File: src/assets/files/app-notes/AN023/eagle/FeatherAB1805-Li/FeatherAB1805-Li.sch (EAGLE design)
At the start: 11 parts, among them Q1 32.768kHz, Q2 2N7002L, U1 XC6215, U2 AB1805

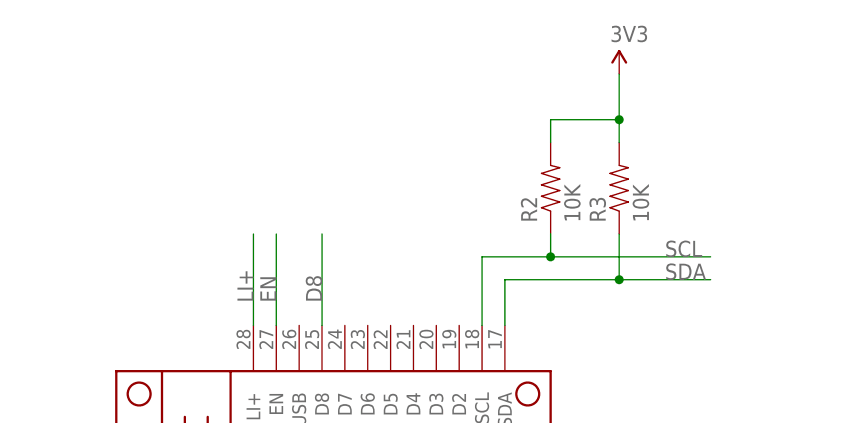
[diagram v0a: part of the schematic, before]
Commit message: Update AB1805-Li design
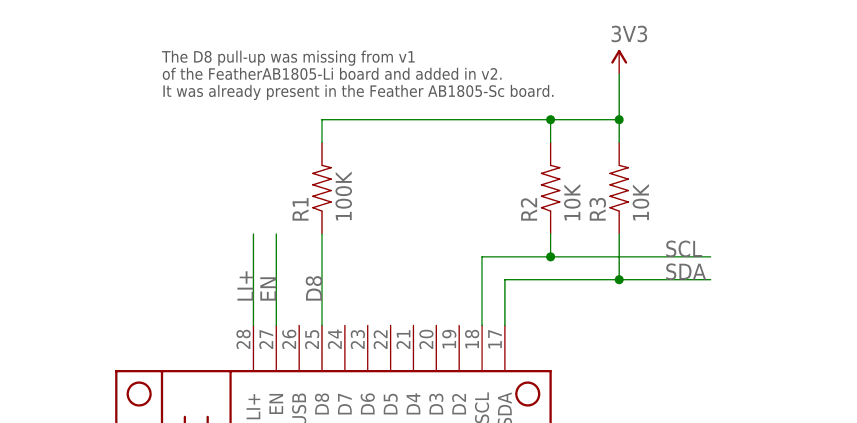
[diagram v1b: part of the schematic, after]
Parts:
- added R1: 100K, rickk2:RES-100K-0603
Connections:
- net 3V3: now also R1.2
- net D8: now also R1.1
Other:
- note added: "The D8 pull-up was missing from v1 of the FeatherAB1805-Li board and added in v2. It was already present in the Feather AB1805-Sc board."
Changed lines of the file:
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@@
 <part name="U1" library="rickk2" deviceset="XC6215" device="" value="XC6215"/>
 <part name="GND3" library="rickk2" deviceset="GND" device=""/>
+<part name="R1" library="rickk2" deviceset="RES-100K-0603" device="" value="100K"/>
 </parts>
 <sheets>
@@
 It's generated from the XC6215 regulator
 and stays on even if EN is pulled low.</text>
+<text x="101.6" y="160.02" size="1.27" layer="97">The D8 pull-up was missing from v1
+of the FeatherAB1805-Li board and added in v2.
+It was already present in the Feather AB1805-Sc board.</text>
 </plain>
 <instances>
@@
 <instance part="GND3" gate="1" x="149.86" y="55.88" smashed="yes">
 <attribute name="VALUE" x="147.32" y="53.34" size="1.778" layer="96"/>
+</instance>
+<instance part="R1" gate="G$1" x="119.38" y="149.86" smashed="yes" rot="R90">
+<attribute name="NAME" x="117.8814" y="146.05" size="1.778" layer="95" rot="R90"/>
+<attribute name="VALUE" x="122.682" y="146.05" size="1.778" layer="96" rot="R90"/>
 </instance>
 </instances>
@@
 <wire x1="119.38" y1="134.62" x2="119.38" y2="144.78" width="0.1524" layer="91"/>
 <label x="119.38" y="137.16" size="1.778" layer="95" rot="R90"/>
+<pinref part="R1" gate="G$1" pin="1"/>
 </segment>
 <segment>
@@
 <junction x="152.4" y="157.48"/>
 <pinref part="SUPPLY2" gate="G$1" pin="3V3"/>
-</segment>
-</net>
+<pinref part="R1" gate="G$1" pin="2"/>
+<wire x1="144.78" y1="157.48" x2="119.38" y2="157.48" width="0.1524" layer="91"/>
+<wire x1="119.38" y1="157.48" x2="119.38" y2="154.94" width="0.1524" layer="91"/>
+<junction x="144.78" y="157.48"/>
+</segment>
+</net>
